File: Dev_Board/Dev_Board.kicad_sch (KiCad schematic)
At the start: 33 parts, among them J1 Conn_01x04, J2 Conn_01x04, J3 Conn_01x04, J4 Conn_01x04

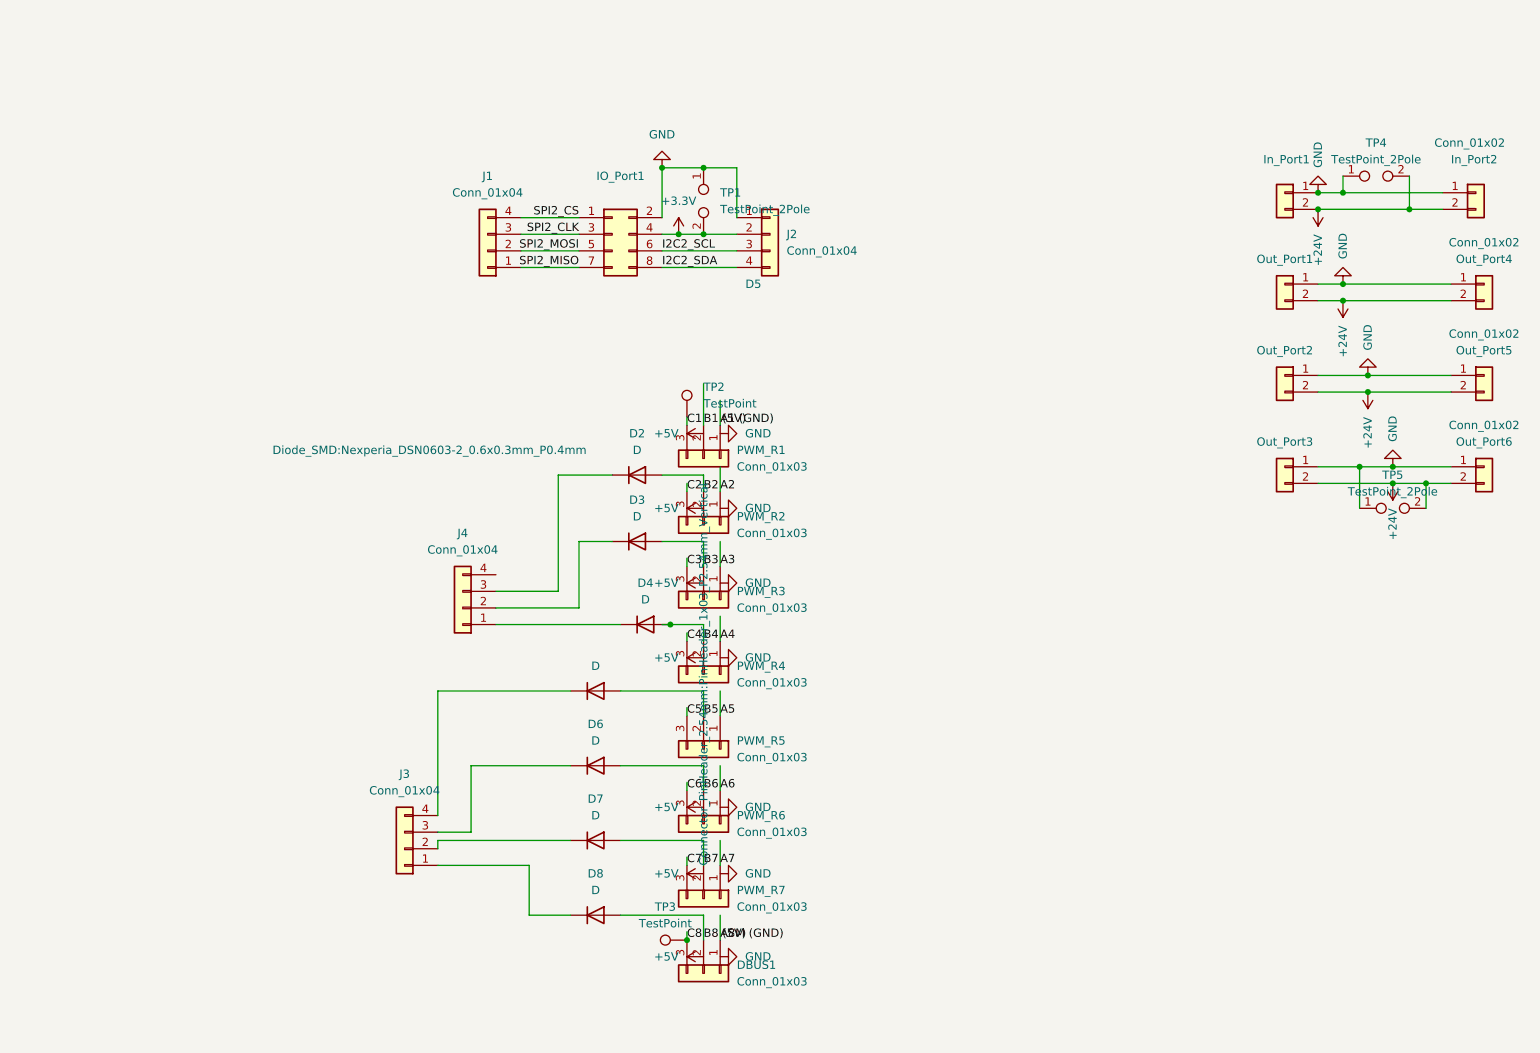
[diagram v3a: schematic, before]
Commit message: fixed the tracks and pin headers and I only added diodes to the 3.3V pins
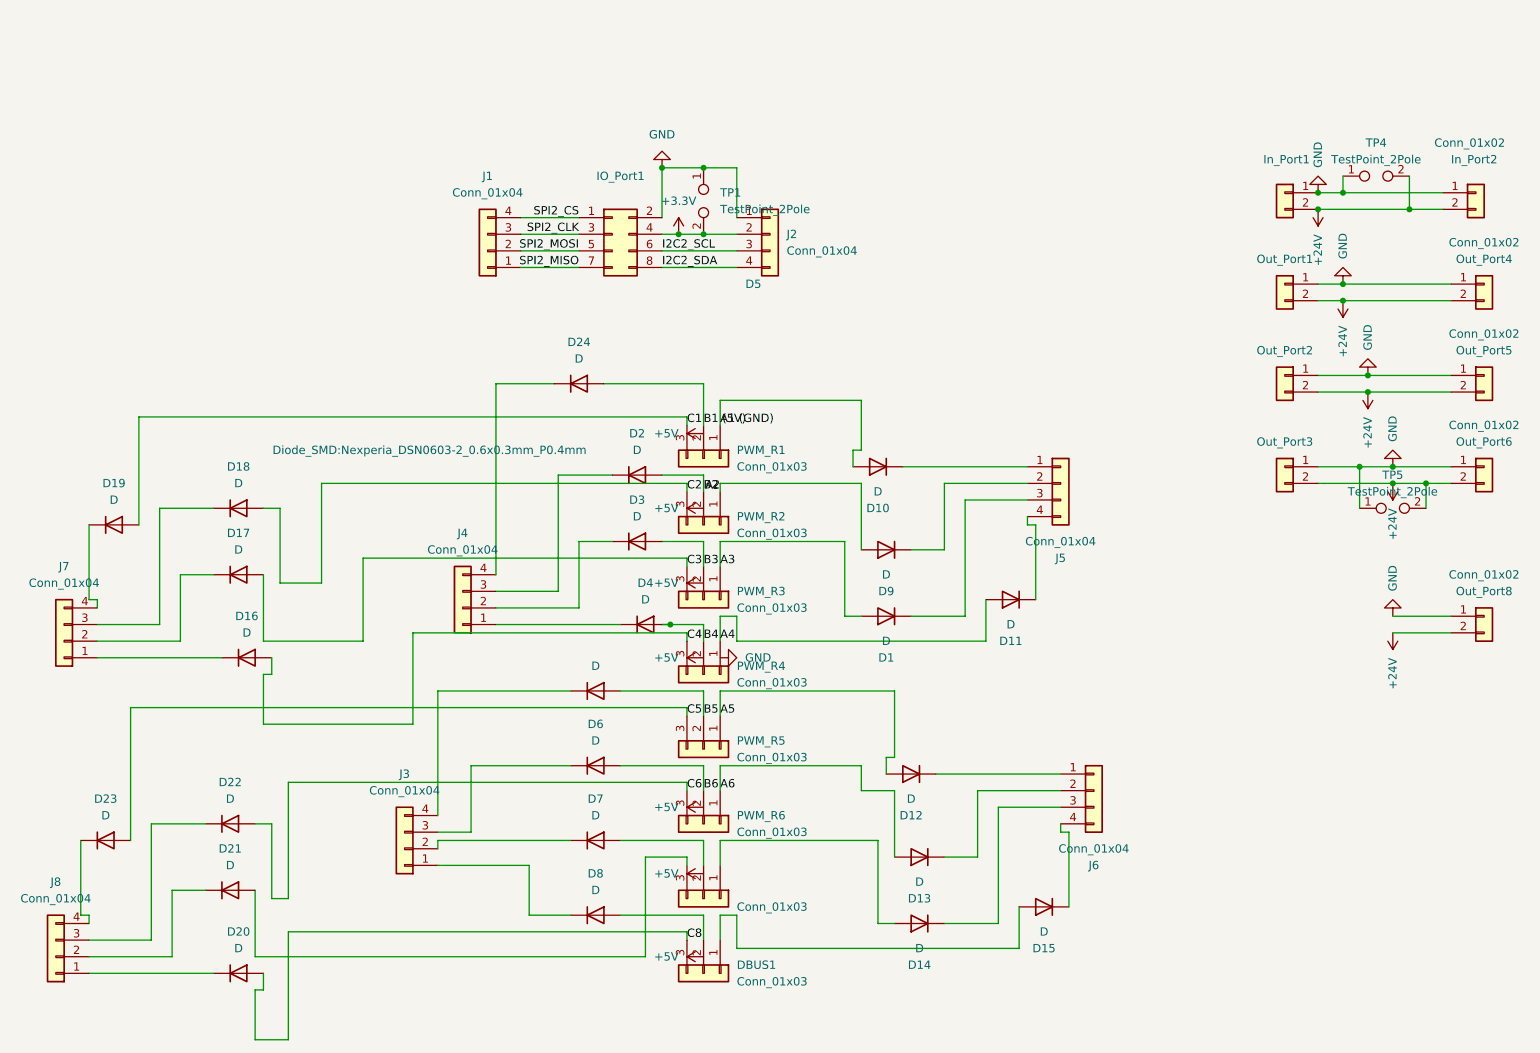
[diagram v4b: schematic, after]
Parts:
- removed TP2, TP3: TestPoint, TestPoint:TestPoint_Pad_2.0x2.0mm, symbol Connector:TestPoint
- added D1, D10, D11, D12, D13, D14, D15, D16, D17, D18, D19, D20, D21, D22, D23, D24, D9: D, Diode_SMD:Nexperia_DSN0603-2_0.6x0.3mm_P0.4mm, symbol Device:D
- added J5, J6, J7, J8: Conn_01x04, Connector_PinHeader_2.54mm:PinHeader_1x04_P2.54mm_Vertical, symbol Connector_Generic:Conn_01x04
- added Out_Port8: Conn_01x02, Connector_AMASS:AMASS_XT30U-F_1x02_P5.0mm_Vertical, symbol Connector_Generic:Conn_01x02
- DBUS1, PWM_R1, PWM_R2, PWM_R3, PWM_R4, PWM_R5, PWM_R6, PWM_R7: footprint Connector_PinHeader_2.54mm:PinHeader_1x03_P2.54mm_Vertical -> Connector_PinSocket_2.54mm:PinSocket_1x03_P2.54mm_Vertical
- IO_Port1: footprint Connector_PinHeader_2.54mm:PinHeader_2x04_P2.54mm_Vertical -> Connector_PinSocket_2.54mm:PinSocket_2x04_P2.54mm_Vertical
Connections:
- net +24V: now also Out_Port8.2 (Pin_2)
- net A1 (GND): now also D10.2 (A)
- net A2: now also D9.2 (A)
- net A3: now also D1.2 (A)
- net A4: now also D11.2 (A)
- net A5: now also D12.2 (A)
- net A6: now also D13.2 (A)
- net B1 (5V): now also D24.2 (A)
- net C1: now also D19.2 (A)
- net C2: now also D18.2 (A)
- net C3: now also D17.2 (A)
- net C4: now also D16.2 (A)
- net C5: now also D23.2 (A)
- net C6: now also D22.2 (A)
- net C8: now also D20.2 (A)
- net GND: now also Out_Port8.1 (Pin_1)
- net at J4.4 (Pin_4): now also D24.1 (K)
- net A7: no longer names the net of PWM_R7.1 (Pin_1)
- net A7: now also D14.2 (A)
- net A8M (GND): no longer names the net of DBUS1.1 (Pin_1)
- net A8M (GND): now also D15.2 (A)
- net B7: no longer names the net of D7.2 (A), PWM_R7.2 (Pin_2)
- net B8 (5V): no longer names the net of D8.2 (A), DBUS1.2 (Pin_2)
- net C7: no longer names the net of PWM_R7.3 (Pin_3)
- net C7: now also D21.2 (A)
- new net: D11.1 (K), J5.4 (Pin_4)
- new net: D16.1 (K), J7.1 (Pin_1)
- new net: D17.1 (K), J7.2 (Pin_2)
- new net: D18.1 (K), J7.3 (Pin_3)
- new net: D19.1 (K), J7.4 (Pin_4)
- new net: D12.1 (K), J6.1 (Pin_1)
- new net: D13.1 (K), J6.2 (Pin_2)
- new net: D14.1 (K), J6.3 (Pin_3)
- new net: D15.1 (K), J6.4 (Pin_4)
- new net: D1.1 (K), J5.3 (Pin_3)
- new net: D10.1 (K), J5.1 (Pin_1)
- new net: D22.1 (K), J8.3 (Pin_3)
- new net: D9.1 (K), J5.2 (Pin_2)
- new net: D20.1 (K), J8.1 (Pin_1)
- new net: D21.1 (K), J8.2 (Pin_2)
- new net: D23.1 (K), J8.4 (Pin_4)
